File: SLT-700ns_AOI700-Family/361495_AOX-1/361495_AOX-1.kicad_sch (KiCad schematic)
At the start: 11 parts, among them U1 12-Pin_SLx_Can

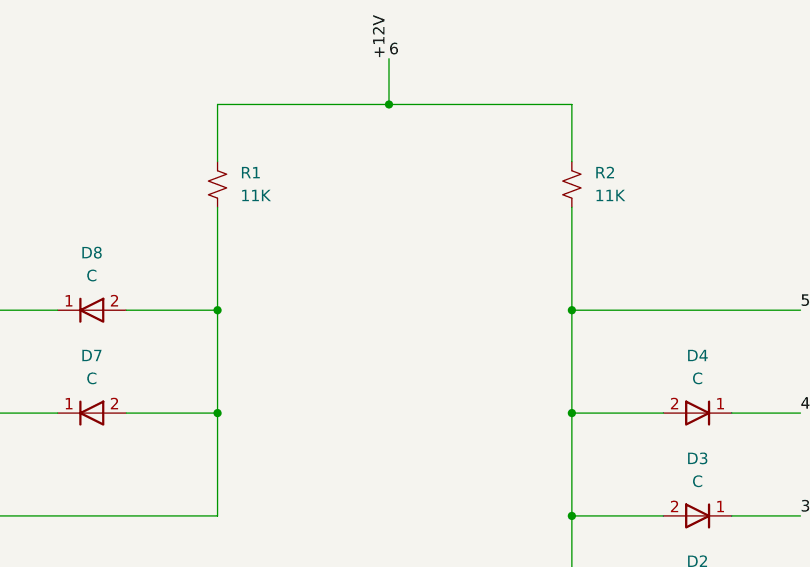
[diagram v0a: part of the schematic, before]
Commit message: Add can P/N to schematics for SLT-700
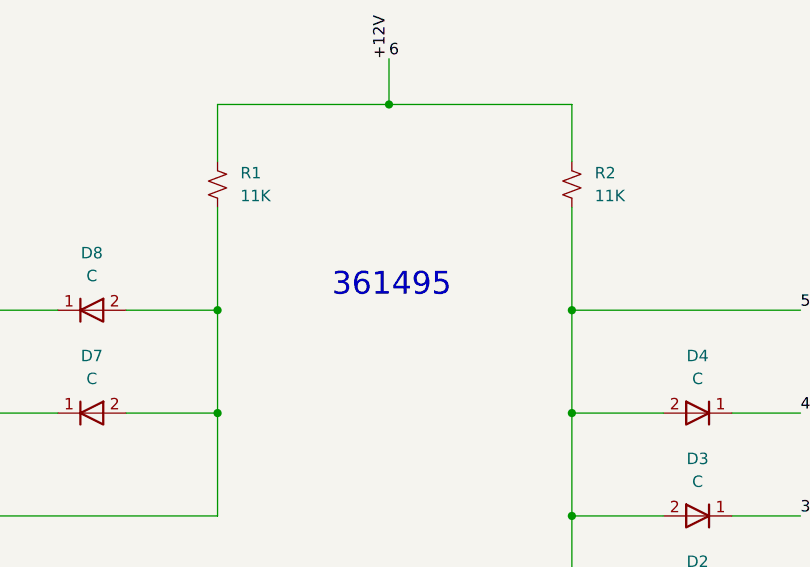
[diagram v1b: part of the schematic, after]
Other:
- note added: "361495"
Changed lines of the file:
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@@
     (stroke (width 0) (type default) (color 0 0 0 0))
+  )
+  (text "361495" (at 111.76 66.04 0)
+    (effects (font (size 2.54 2.54)) (justify left bottom))
   )
   (text "All Diodes \"C\"" (at 111.76 133.35 0)
